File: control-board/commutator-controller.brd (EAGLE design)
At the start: 43 x 95 mm, 39 parts, among them U1 PTN04050C, U2 LTC4425EMSE#PBF, U3 IS31FL3193, U4 TMC2130, U5 TEENSY-3.2

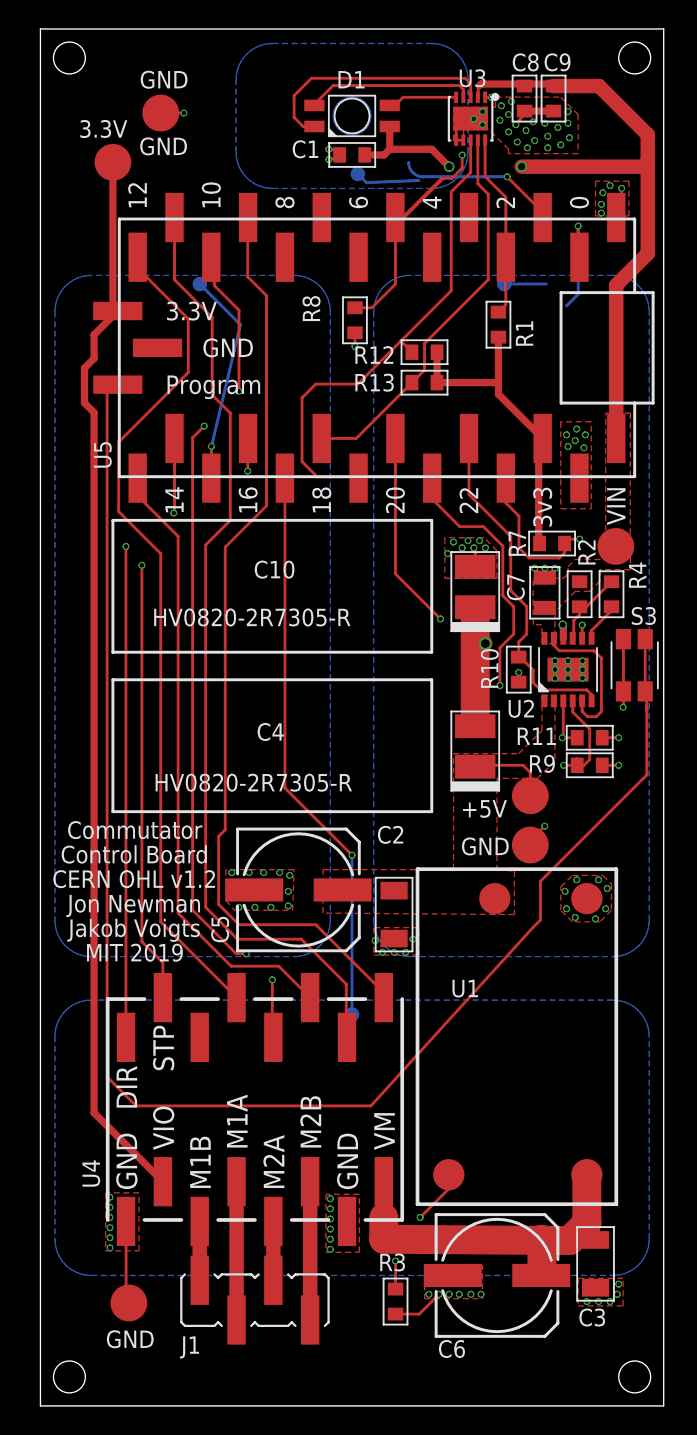
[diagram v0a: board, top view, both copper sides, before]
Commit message: Small changes to the commutator driver board
- No change in BOM or functionality
- Added silkscreen outline to LED touch pad
- Added OE logo
- Remove license from silkscreen
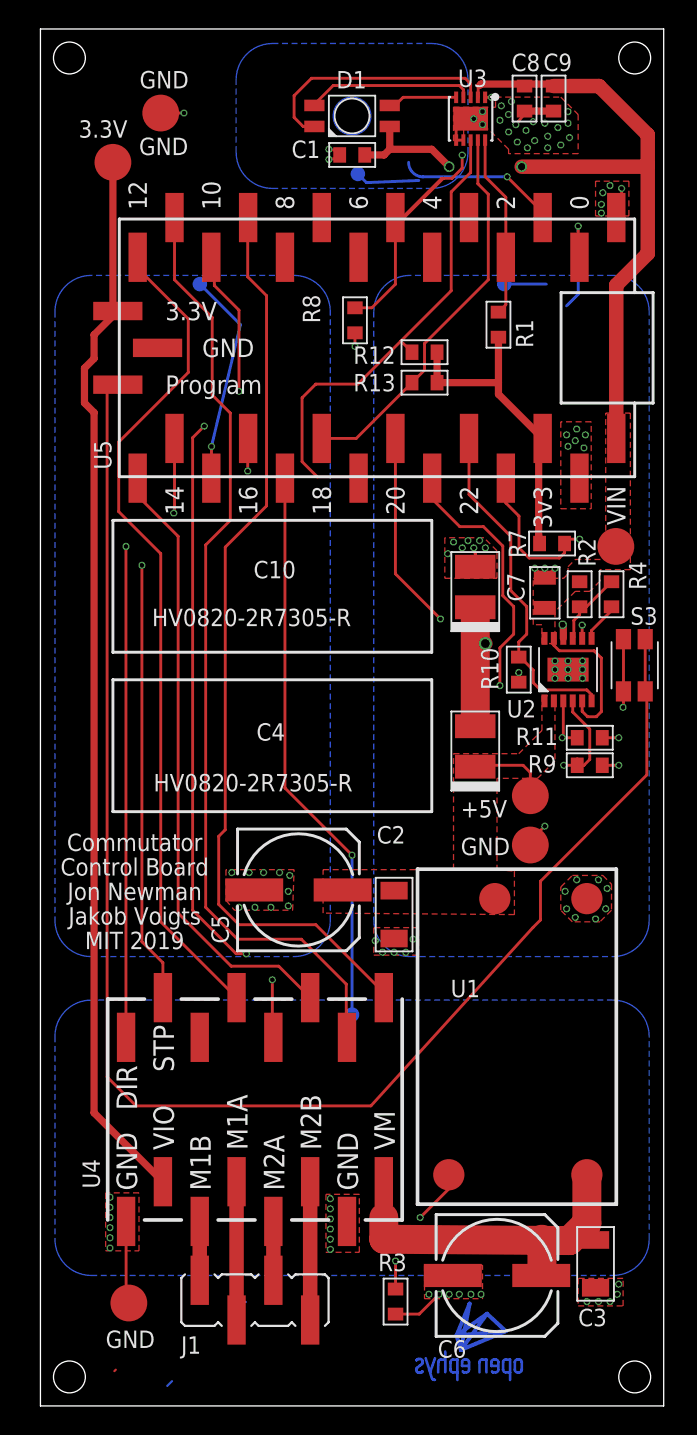
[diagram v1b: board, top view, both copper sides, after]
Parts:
- added X1: OE-LOGO_7X5, jonnew:OE-LOGO-7X5
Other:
- board text added: "Commutator Control Board Jon Newman Jakob Voigts MIT 2019"
- board text added: "Commutator v1.1"
- board text removed: "Commutator Control Board CERN OHL v1.2 Jon Newman Jakob Voigts MIT 2019"
- board text removed: "Commutator v1.1 OHL v1.2"

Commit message: Small fixes to control board for production
- Vias under LED driver were not symmetrical which caused delta-T during
reflow and therefore bad settling of device. I made them symmetrical
- Removed a couple random copper lines
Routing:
- net MODE: track 15.5 -> 14.4 mm
- net GND: vias 107 -> 109
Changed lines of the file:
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@@
 <setting verticaltext="up"/>
 </settings>
-<grid distance="0.5" unitdist="mm" unit="mm" style="lines" multiple="1" display="yes" altdistance="5" altunitdist="mil" altunit="mil"/>
+<grid distance="0.1" unitdist="mm" unit="mm" style="lines" multiple="1" display="yes" altdistance="5" altunitdist="mil" altunit="mil"/>
 <layers>
 <layer number="1" name="Top" color="4" fill="1" visible="yes" active="yes"/>
@@
 <contactref element="C9" pad="2"/>
 <via x="31.7" y="88.7" extent="1-16" drill="0.3"/>
-<via x="29.9" y="88.8" extent="1-16" drill="0.3"/>
+<via x="29.7" y="88.8" extent="1-16" drill="0.3"/>
 <contactref element="R8" pad="2"/>
 <via x="32.8" y="88.4" extent="1-16" drill="0.3"/>
@@
 <wire x1="40.225" y1="49.3" x2="40.225" y2="48.225" width="0.2" layer="1"/>
 <wire x1="40.225" y1="48.225" x2="40.2" y2="48.2" width="0.2" layer="1"/>
+<via x="28.9" y="89.3" extent="1-16" drill="0.3"/>
+<via x="28.9" y="88.4" extent="1-16" drill="0.3"/>
 <wire x1="21.7" y1="73.1" x2="8.08" y2="73" width="0" layer="19" extent="1-1"/>
 </signal>
@@
 </polygon>
 <via x="32.2" y="84.8" extent="1-16" drill="0.3"/>
-<wire x1="21.9" y1="85" x2="22.5" y2="84.4" width="0.2" layer="16"/>
-<wire x1="26.102121875" y1="84.548540625" x2="22.5" y2="84.4" width="0.2" layer="16"/>
 <contactref element="U5" pad="1"/>
-<wire x1="32.2" y1="84.8" x2="26.4" y2="84.8" width="0.2" layer="16"/>
-<wire x1="26.4" y1="84.8" x2="25.4" y2="85.8" width="0.2" layer="16" curve="-90"/>
+<wire x1="26.6" y1="84.8" x2="32.2" y2="84.8" width="0.2" layer="16"/>
+<wire x1="26.6" y1="84.8" x2="26.4" y2="84.8" width="0.2" layer="16"/>
 <wire x1="34.65" y1="81.99" x2="34.65" y2="82.35" width="0.2" layer="1"/>
 <wire x1="34.65" y1="82.35" x2="32.2" y2="84.8" width="0.2" layer="1"/>
+<wire x1="21.9" y1="85" x2="22.1" y2="84.8" width="0.2" layer="16"/>
+<wire x1="22.1" y1="84.8" x2="26.6" y2="84.8" width="0.2" layer="16"/>
 </signal>
 <signal name="N$13">
@@
 </polygon>
 </signal>
-<signal name="N$4">
-<wire x1="5.2" y1="2.5" x2="5.1" y2="2.4" width="0.1524" layer="1"/>
-</signal>
-<signal name="N$12">
-<wire x1="14.17" y1="7.16" x2="14.14" y2="7.19" width="0.1524" layer="16"/>
-</signal>
-<signal name="N$15">
-<wire x1="9.08" y1="1.71" x2="8.75" y2="1.38" width="0.1524" layer="16"/>
-</signal>
 </signals>
